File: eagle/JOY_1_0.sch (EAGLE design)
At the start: 11 parts, among them U1 JOYSTICKPTH, X1 Out Y~, X2 Out X~, X3 Out Z

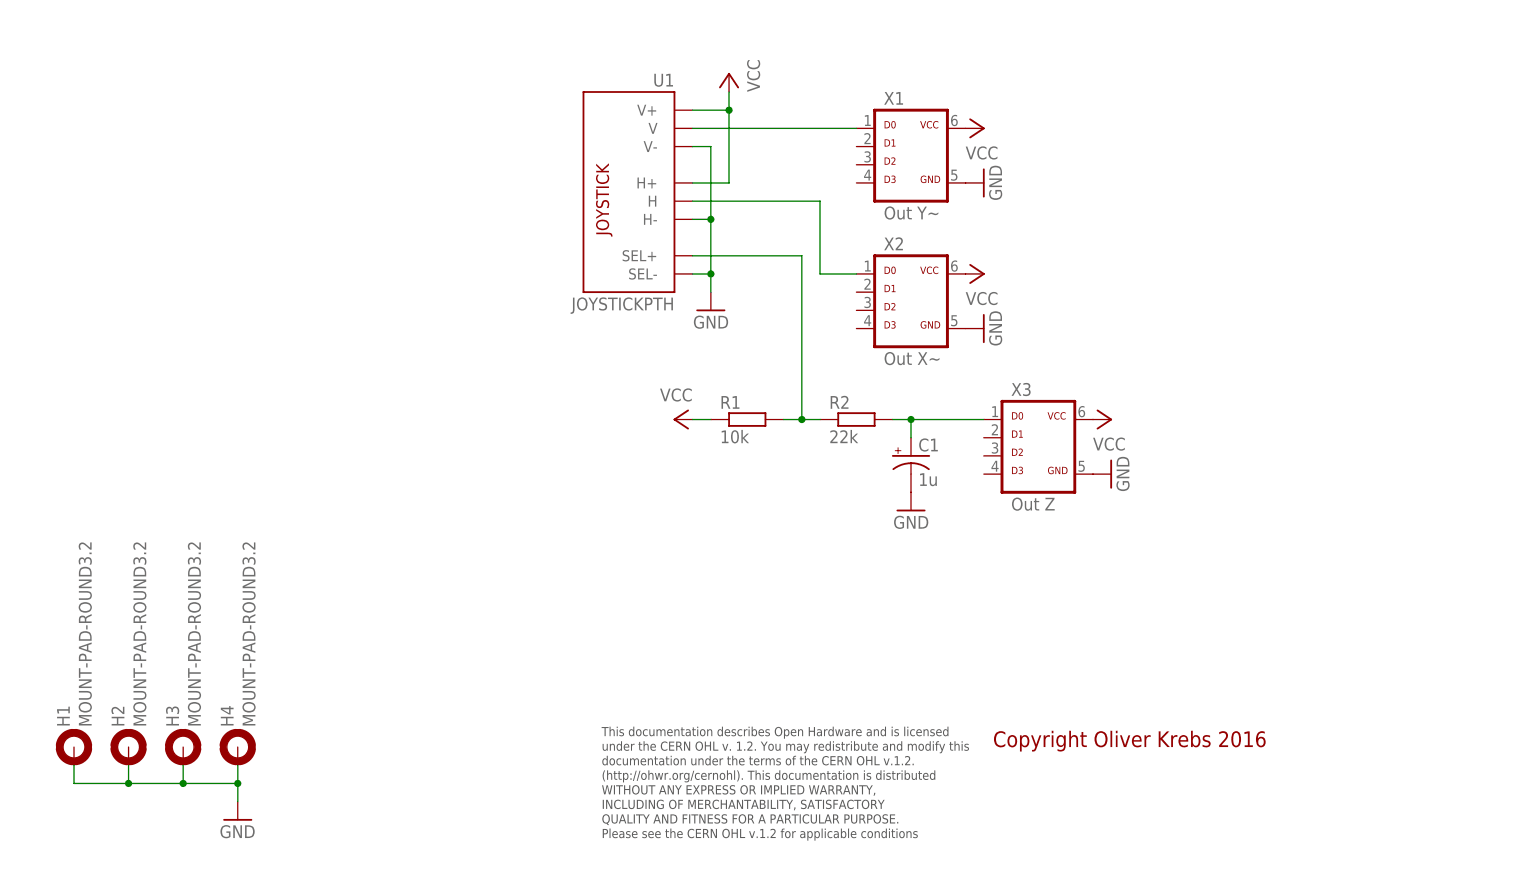
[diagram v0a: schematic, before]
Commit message: Add new tetra-Board and arduino files
Add AMP_1_0, AVC_1_0, D18_1_1, IOP_1_2, MIC_1_0, PIN_1_1, POT_1_0, PWA_1_0, PWR_1_0, RGF 2.0, SOC_2_0, VLT_1_0
Add mex_nano_shield_keyboard, mex_nano_shied_numbers

New arduino projects
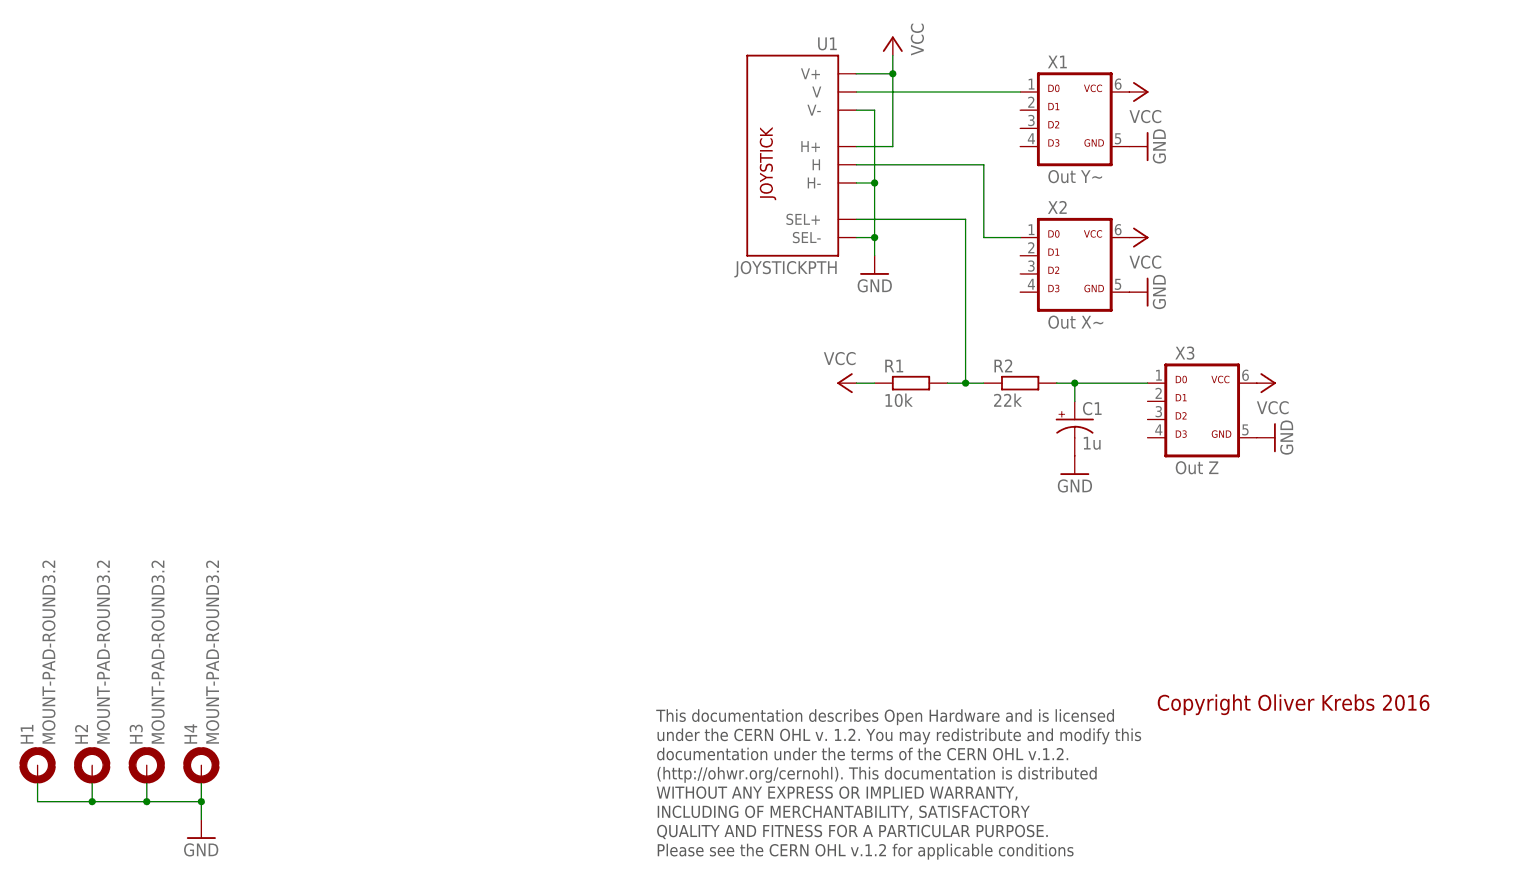
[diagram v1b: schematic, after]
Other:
- moved on the sheet: C1, H1, H2, H3, H4, R1, R2, U1, X1, X2, X3
